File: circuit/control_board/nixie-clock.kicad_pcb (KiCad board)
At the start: 2 copper layers, 102.4 x 50.8 mm, 45 parts, among them IC1 ATMEGA328-P, P1 CONN_2, P10 CONN_2, P2 CONN_2, P3 CONN_4, P4 CONN_4, P5 CONN_8, P6 CONN_12, P7 CONN_2, P8 CONN_2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

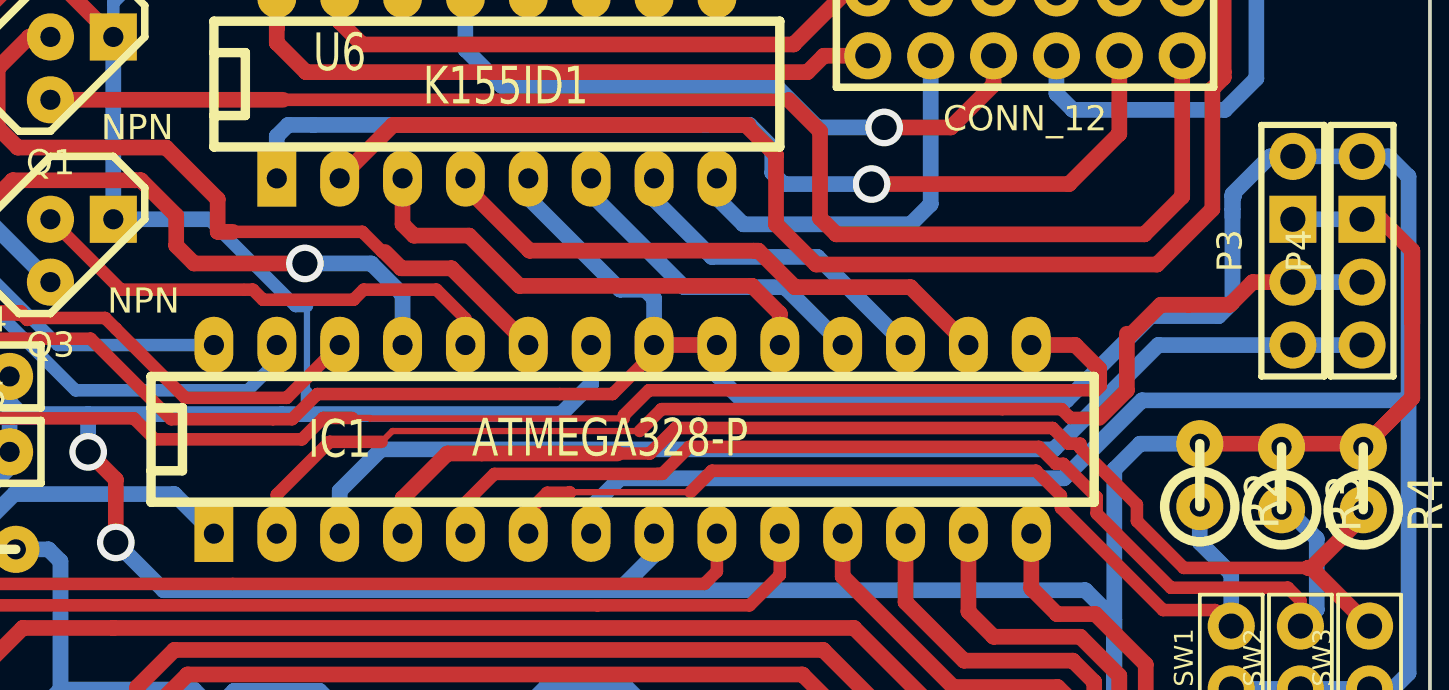
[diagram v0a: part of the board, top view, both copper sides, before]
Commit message: Control board: Optimize FTDI route
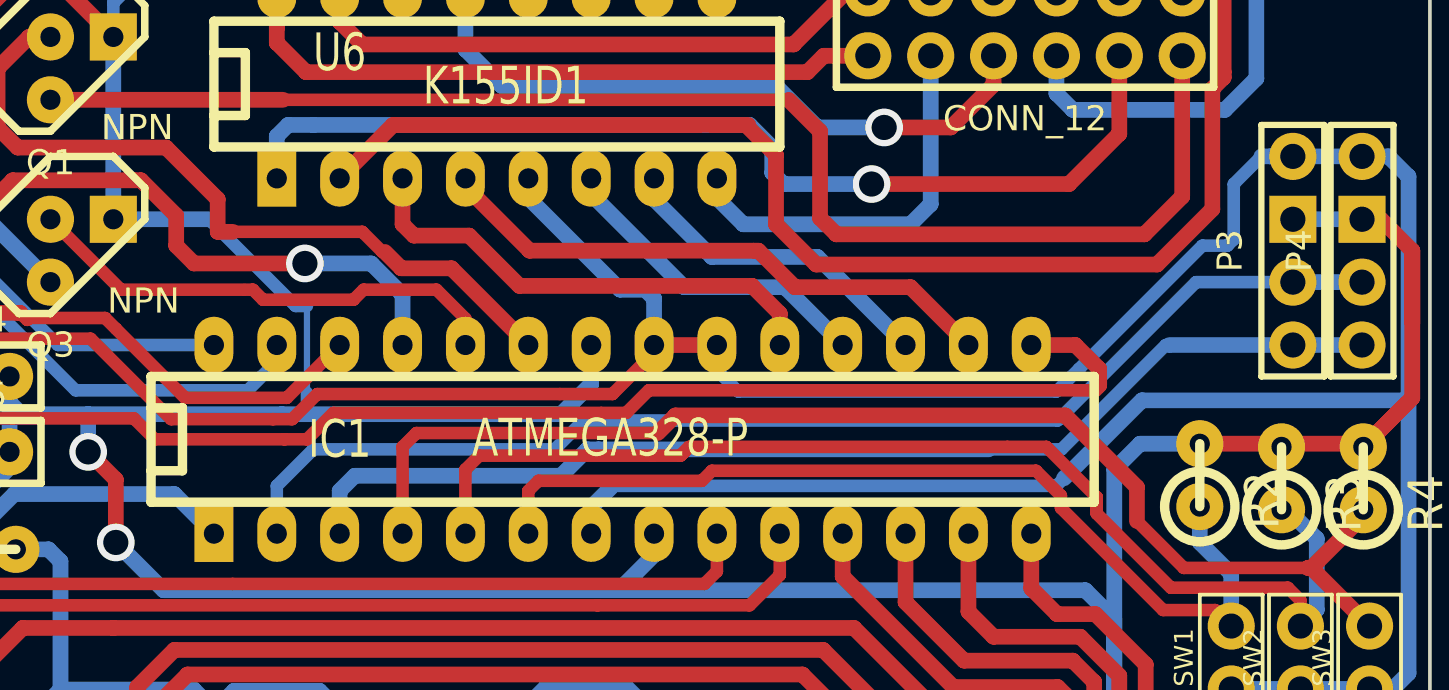
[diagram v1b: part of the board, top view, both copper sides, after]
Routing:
- net Mode button: track 55.3 -> 57.2 mm
- net Adjust button: track 45.6 -> 47.6 mm
- net 5V: track 239.7 -> 238.0 mm
- net Bluetooth/FTDI Tx: track 50.7 -> 49.2 mm
- net Search button: track 39.1 -> 40.5 mm

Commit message: Control board: Optimize the GND route
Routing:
- net GND: track 321.0 -> 359.6 mm, vias 2 -> 3
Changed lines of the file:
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@@
     (thickness 1.6)
     (drawings 7)
-    (tracks 870)
+    (tracks 873)
     (zones 0)
     (modules 45)
@@
   (layers
     (15 F.Cu signal)
-    (0 B.Cu signal hide)
+    (0 B.Cu signal)
     (16 B.Adhes user)
     (17 F.Adhes user)
@@
   )
   (setup
-    (last_trace_width 0.508)
+    (last_trace_width 0.635)
     (user_trace_width 0.508)
     (user_trace_width 0.635)
@@
   (segment (start 168.5036 103.9876) (end 186.436 103.9876) (width 0.508) (layer B.Cu) (net 2))
   (segment (start 186.436 103.9876) (end 186.7408 103.6828) (width 0.508) (layer B.Cu) (net 2))
-  (segment (start 172.72 98.298) (end 172.72 99.314) (width 0.508) (layer B.Cu) (net 2) (status C00000))
-  (segment (start 172.72 99.314) (end 173.5836 100.1776) (width 0.508) (layer B.Cu) (net 2) (status 400000))
+  (segment (start 172.72 98.298) (end 172.72 99.314) (width 0.508) (layer B.Cu) (net 2))
+  (segment (start 172.72 99.314) (end 173.5836 100.1776) (width 0.508) (layer B.Cu) (net 2))
   (segment (start 186.436 100.1776) (end 187.3504 99.2632) (width 0.508) (layer B.Cu) (net 2))
   (segment (start 173.5836 100.1776) (end 186.436 100.1776) (width 0.508) (layer B.Cu) (net 2))
-  (segment (start 194.7164 90.678) (end 195.9864 90.678) (width 0.635) (layer B.Cu) (net 2) (status 800000))
+  (segment (start 194.7164 90.678) (end 195.9864 90.678) (width 0.635) (layer B.Cu) (net 2))
   (segment (start 125.2728 98.552) (end 125.3236 98.552) (width 0.508) (layer F.Cu) (net 2))
   (segment (start 170.18 98.6028) (end 168.5036 100.2792) (width 0.508) (layer F.Cu) (net 2))
@@
   (segment (start 183.6928 102.5144) (end 167.9448 102.5144) (width 0.635) (layer B.Cu) (net 4))
   (segment (start 195.9864 98.298) (end 198.7804 98.298) (width 0.635) (layer B.Cu) (net 4))
-  (segment (start 195.9864 95.758) (end 192.0748 95.758) (width 0.508) (layer B.Cu) (net 5) (status 400000))
-  (segment (start 154.94 103.9876) (end 154.94 105.918) (width 0.508) (layer B.Cu) (net 5) (status 800000))
+  (segment (start 195.9864 95.758) (end 192.0748 95.758) (width 0.508) (layer B.Cu) (net 5))
+  (segment (start 154.94 103.9876) (end 154.94 105.918) (width 0.508) (layer B.Cu) (net 5))
   (segment (start 156.4132 102.5144) (end 154.94 103.9876) (width 0.508) (layer B.Cu) (net 5))
   (segment (start 166.1668 102.5144) (end 156.4132 102.5144) (width 0.508) (layer B.Cu) (net 5))
@@
   (segment (start 175.8696 95.9612) (end 180.5432 95.9612) (width 0.635) (layer F.Cu) (net 16))
   (segment (start 174.1932 94.488) (end 174.3964 94.488) (width 0.635) (layer F.Cu) (net 16))
+  (segment (start 150.622 82.189702) (end 150.622 82.0928) (width 0.635) (layer B.Cu) (net 17))
+  (segment (start 101.854 82.296) (end 101.854 84.074) (width 0.635) (layer F.Cu) (net 17) (status 800000))
+  (segment (start 103.9368 80.2132) (end 101.854 82.296) (width 0.635) (layer F.Cu) (net 17))
+  (segment (start 145.542 80.2132) (end 103.9368 80.2132) (width 0.635) (layer F.Cu) (net 17))
+  (segment (start 146.6596 81.3308) (end 145.542 80.2132) (width 0.635) (layer F.Cu) (net 17))
+  (via (at 146.6596 81.3308) (size 1.524) (drill 1.016) (layers F.Cu B.Cu) (net 17))
+  (segment (start 149.86 81.3308) (end 146.6596 81.3308) (width 0.635) (layer B.Cu) (net 17))
+  (segment (start 150.622 82.0928) (end 149.86 81.3308) (width 0.635) (layer B.Cu) (net 17))
   (segment (start 200.8124 94.488) (end 200.8124 100.4316) (width 0.635) (layer F.Cu) (net 17))
   (segment (start 200.8124 100.4316) (end 198.8312 102.4128) (width 0.635) (layer F.Cu) (net 17))
@@
   (segment (start 188.7728 103.3272) (end 188.7728 114.554) (width 0.635) (layer B.Cu) (net 17))
   (segment (start 192.2272 102.2858) (end 189.8142 102.2858) (width 0.635) (layer B.Cu) (net 17))
-  (segment (start 156.1592 96.7232) (end 155.702 96.7232) (width 0.508) (layer B.Cu) (net 17))
-  (segment (start 155.702 96.7232) (end 152.1968 93.218) (width 0.508) (layer B.Cu) (net 17))
-  (segment (start 148.336 93.218) (end 152.1968 93.218) (width 0.635) (layer B.Cu) (net 17))
-  (segment (start 156.1592 96.7232) (end 156.1592 100.2284) (width 0.254) (layer B.Cu) (net 17))
-  (segment (start 156.1592 101.092) (end 156.1592 100.2284) (width 0.508) (layer B.Cu) (net 17))
   (segment (start 152.4 98.298) (end 146.1008 98.298) (width 0.508) (layer B.Cu) (net 18))
   (segment (start 142.0368 94.234) (end 139.192 94.234) (width 0.508) (layer B.Cu) (net 18))
@@
   (segment (start 159.3088 94.5388) (end 159.9692 95.1992) (width 0.635) (layer F.Cu) (net 25))
   (segment (start 159.9692 95.1992) (end 162.0012 95.1992) (width 0.635) (layer F.Cu) (net 25))
-  (segment (start 165.1 105.918) (end 165.1 104.1908) (width 0.508) (layer F.Cu) (net 26) (status 400000))
+  (segment (start 165.1 105.918) (end 165.1 104.1908) (width 0.508) (layer F.Cu) (net 26))
   (segment (start 165.5064 103.7844) (end 172.1104 103.7844) (width 0.508) (layer F.Cu) (net 26))
   (segment (start 165.1 104.1908) (end 165.5064 103.7844) (width 0.508) (layer F.Cu) (net 26))

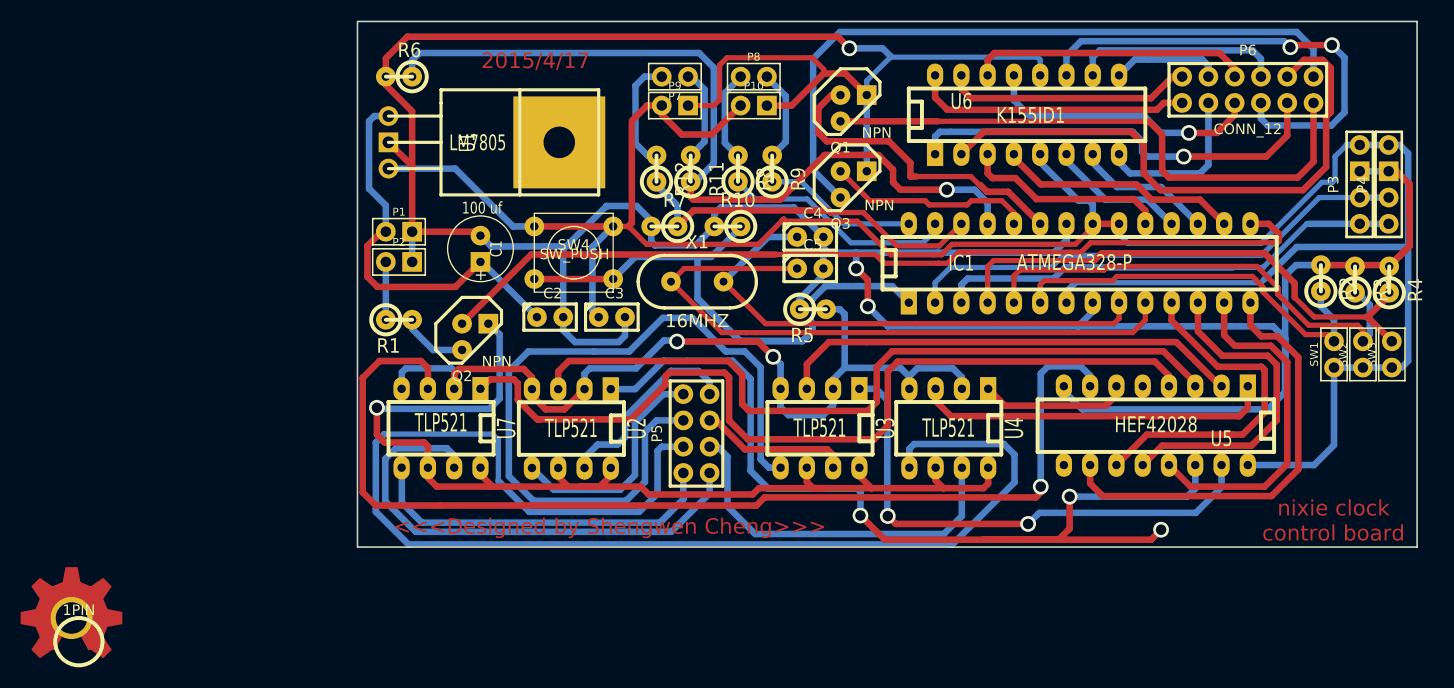
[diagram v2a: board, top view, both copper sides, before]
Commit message: Control board: Finish board optimization
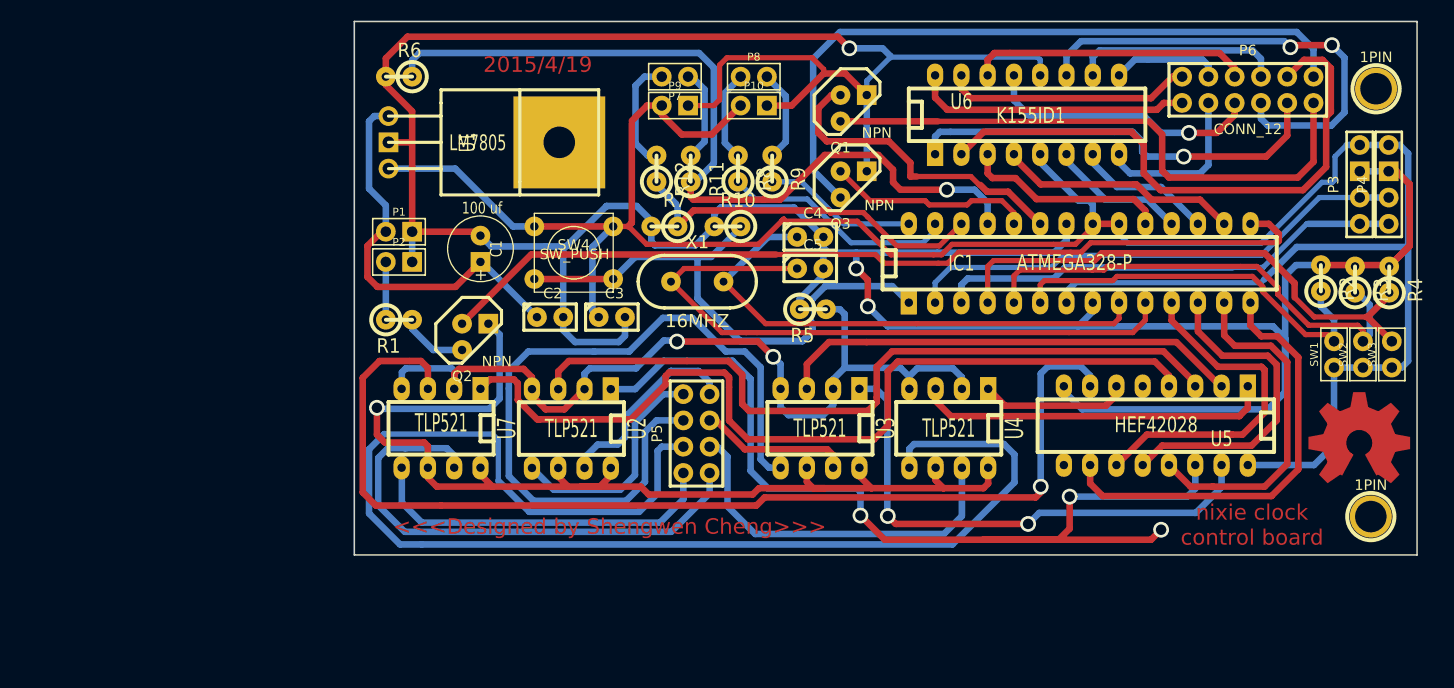
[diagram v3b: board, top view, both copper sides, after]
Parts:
- removed the 1PIN at (72.2, 138.7)
- added 1PIN: P***, Connect:1pin, F.Cu at (197.1, 126.6)
- added 1PIN: P***, Connect:1pin, F.Cu at (197.6, 85.2)
- moved OSHW_COPPER_10MM 125.6 mm to (195.9, 119.5)
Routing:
- net Net-(P5-Pad1): track 48.6 -> 50.3 mm
- net Net-(P5-Pad4): track 128.0 -> 129.0 mm
- net GND: track 359.6 -> 358.8 mm
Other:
- board size 102.4 x 50.8 mm -> 102.7 x 51.6 mm
- board text added: "2015/4/19"
- board text removed: "2015/4/17"

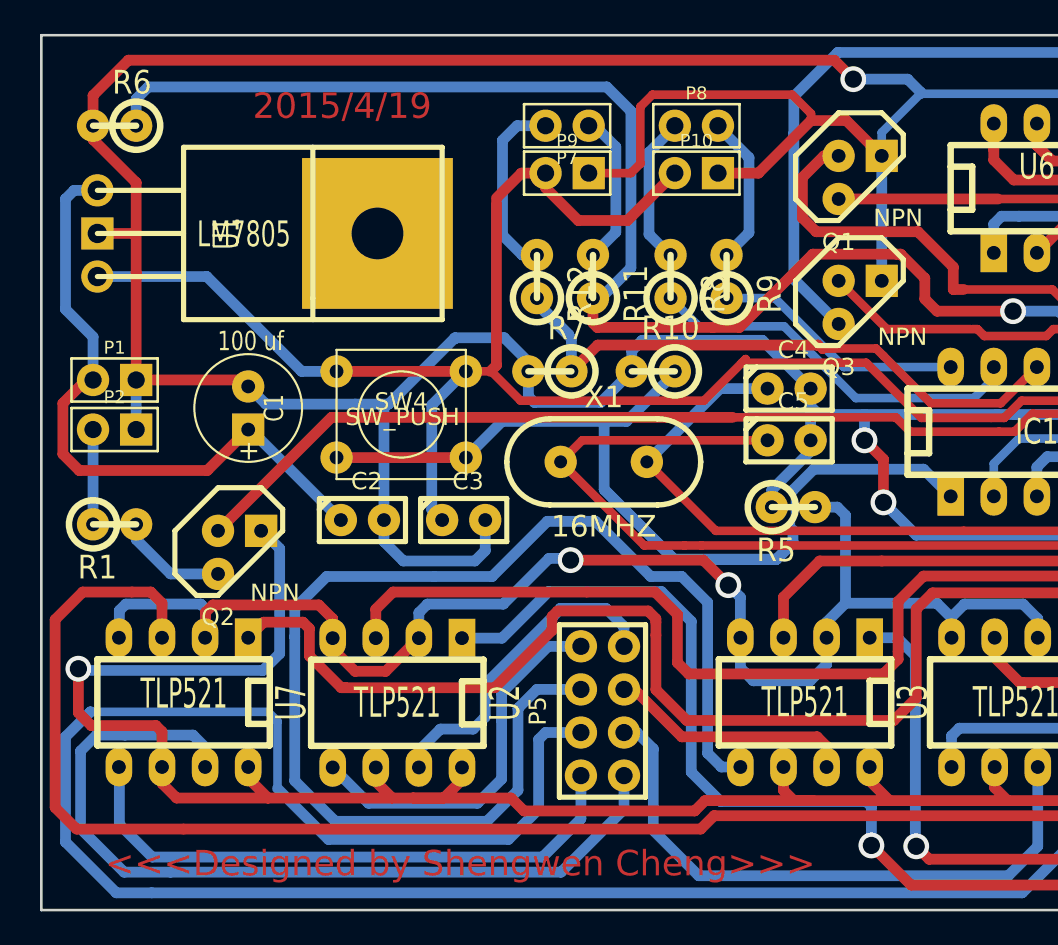
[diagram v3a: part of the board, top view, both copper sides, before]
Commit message: Control board: Fix missing not optimized track line
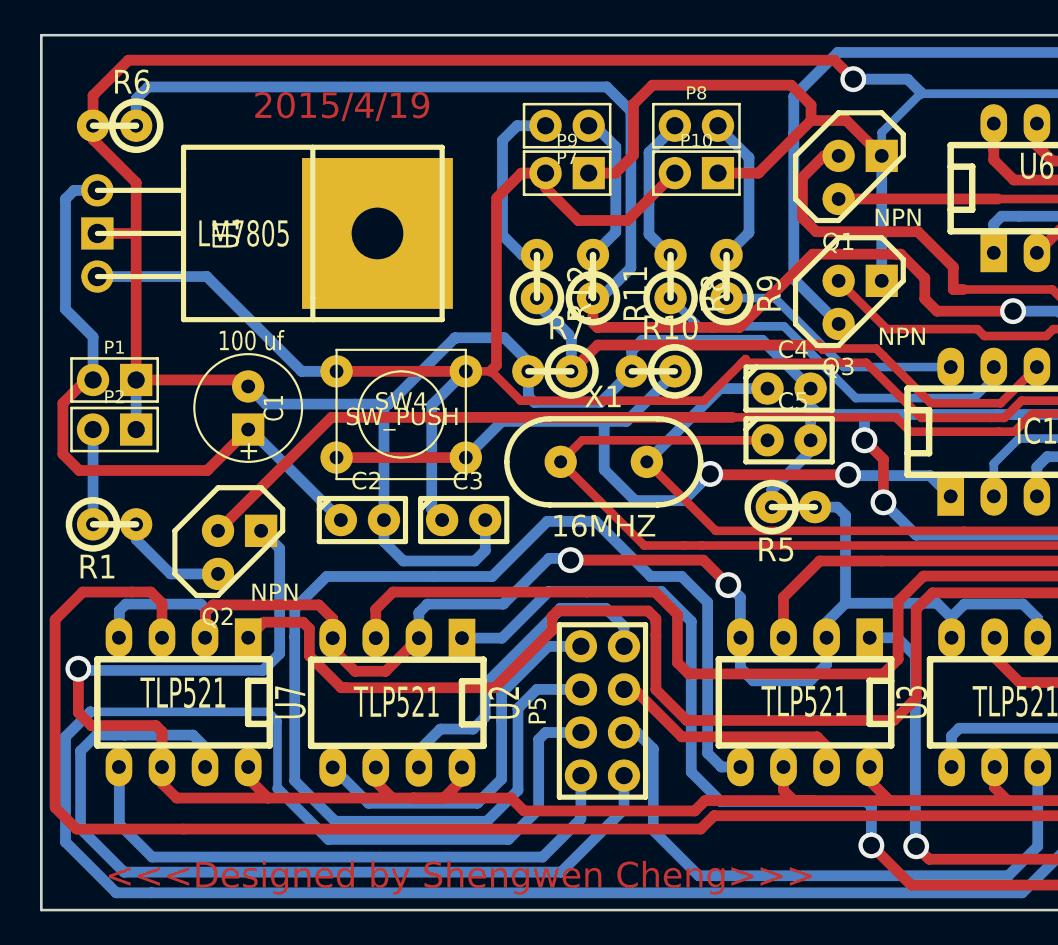
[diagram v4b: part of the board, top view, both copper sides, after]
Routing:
- net Reset: track 85.6 -> 47.3 mm, vias 0 -> 2
- net GND: track 358.8 -> 359.3 mm

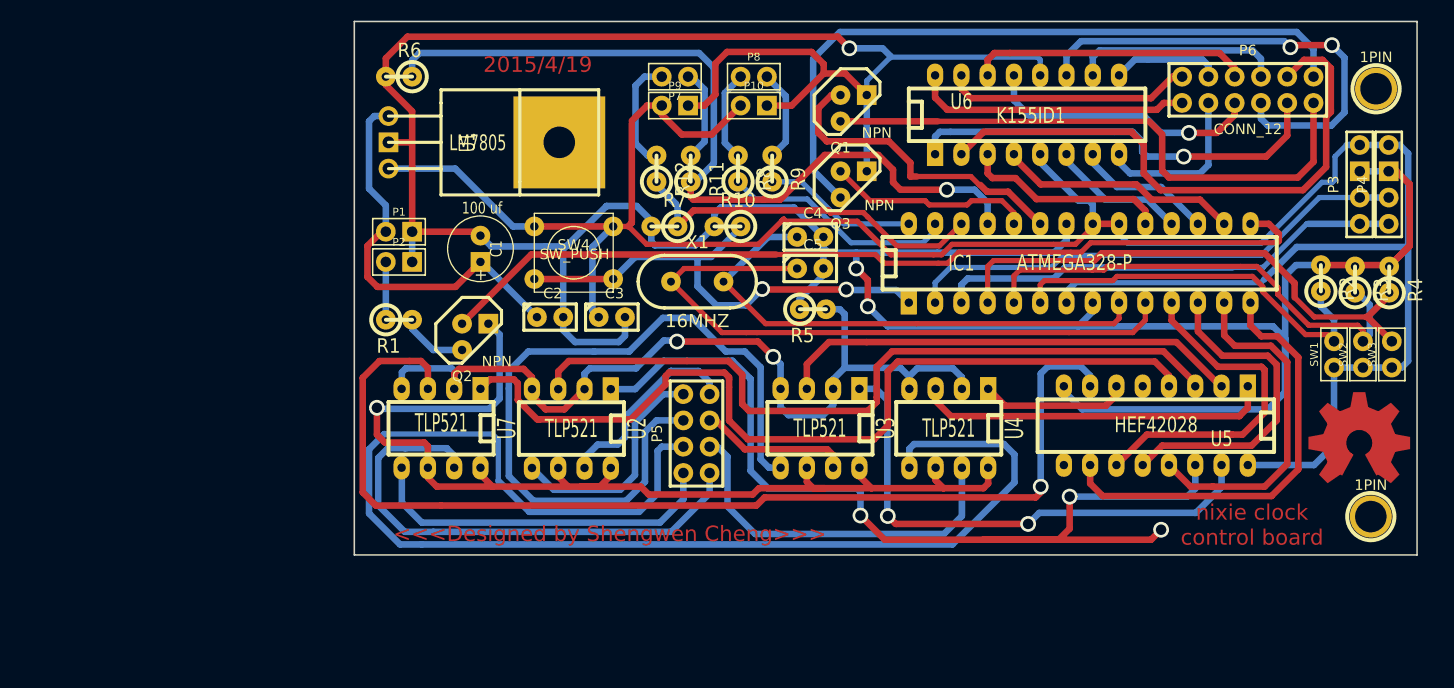
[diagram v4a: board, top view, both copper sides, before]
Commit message: Control board: Optimze some routes
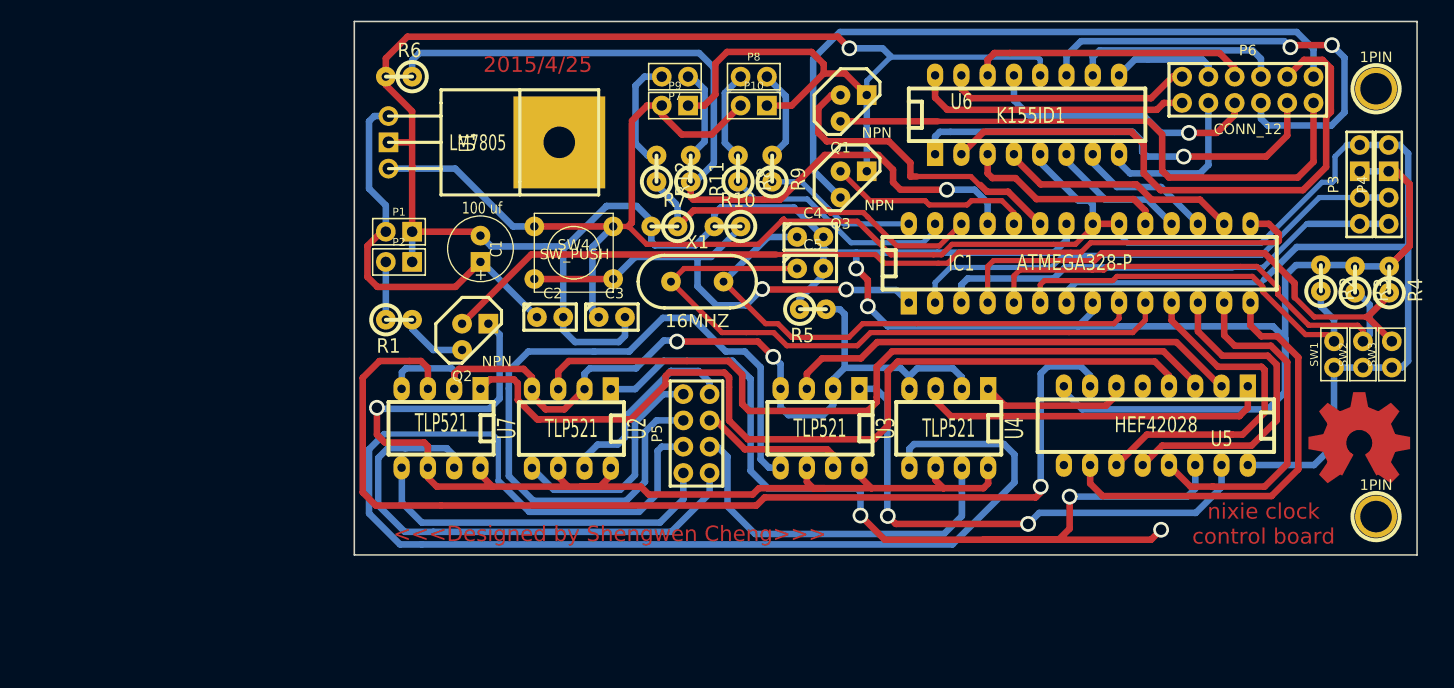
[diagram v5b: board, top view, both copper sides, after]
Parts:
- moved 1PIN 0.51 mm to (197.6, 126.6)
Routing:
- net GND: track 359.3 -> 352.7 mm
- net Crystal1: track 50.5 -> 51.6 mm
- net Crystal2: track 62.8 -> 63.8 mm
- net Net-(U3-Pad3): track 45.2 -> 44.7 mm
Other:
- board text added: "2015/4/25"
- board text removed: "2015/4/19"
